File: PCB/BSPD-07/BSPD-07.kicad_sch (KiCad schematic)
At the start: 50 parts, among them IC1 LM393LVQDRQ1, IC2 LM393LVQDRQ1, IC3 LM393LVQDRQ1, IC4 LDO40LPU50RY, IC5 74LVC1G02GW-Q100H, J1 DTM13-12PA, Q1 RSQ025P03HZGTR, Q2 RJU002N06FRAT106, Q3 RJU002N06FRAT106, U2 TLP175A / COMUS AB38-Q

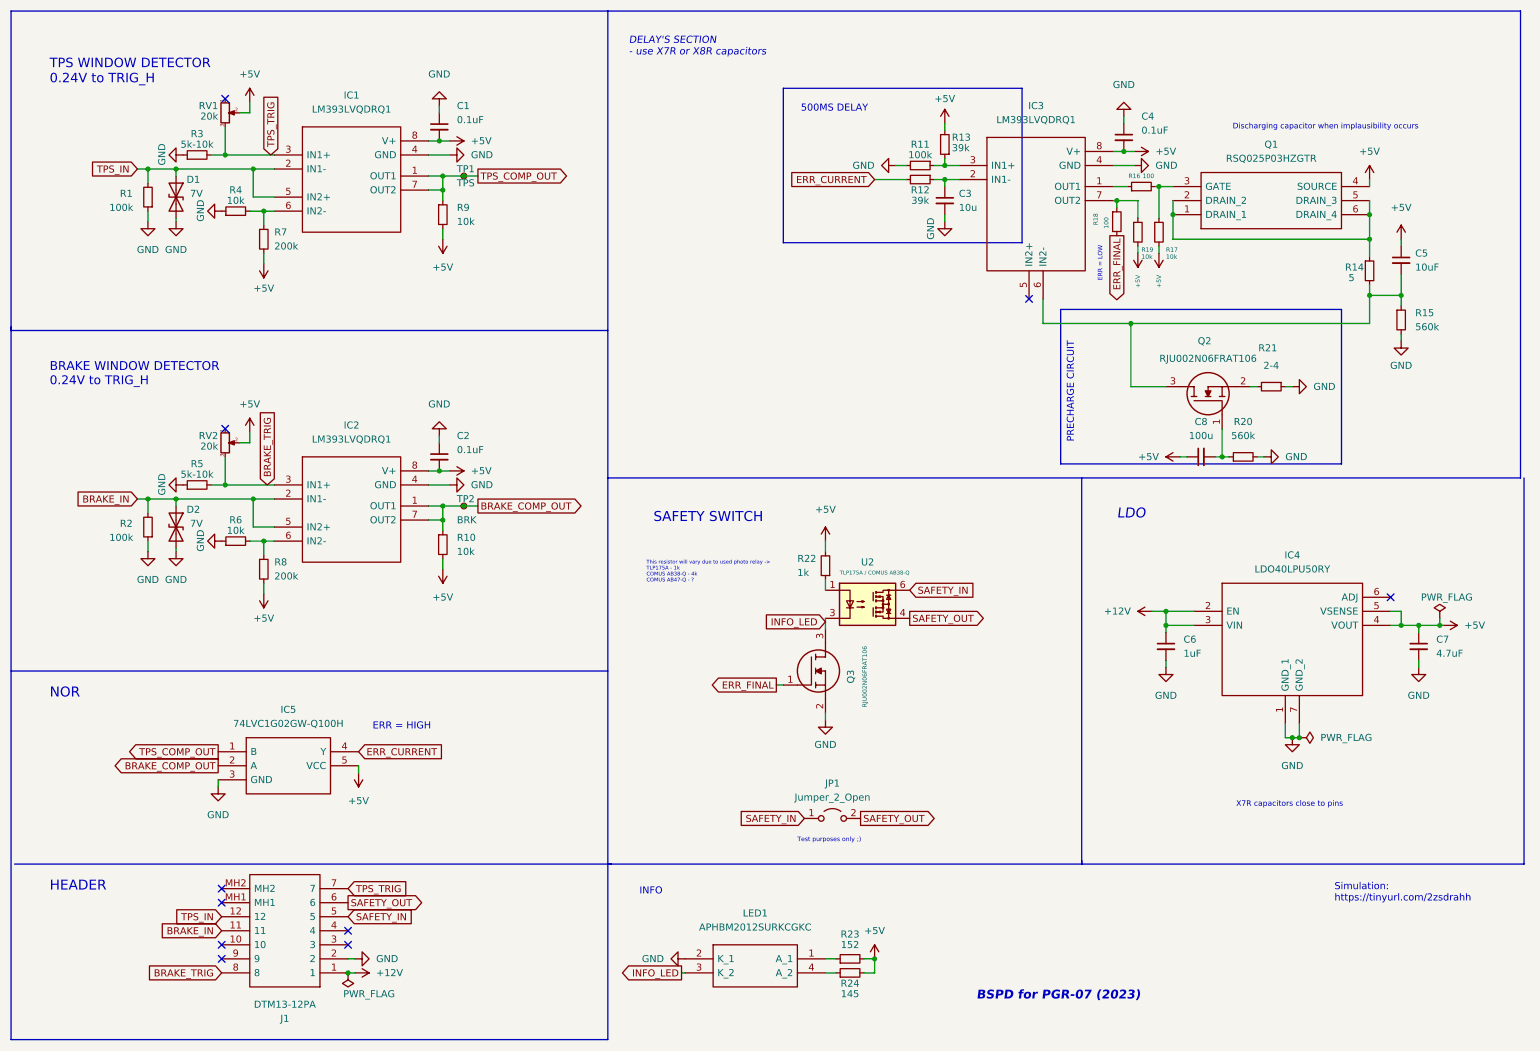
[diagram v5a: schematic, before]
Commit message: Fixed delay resistor reference value
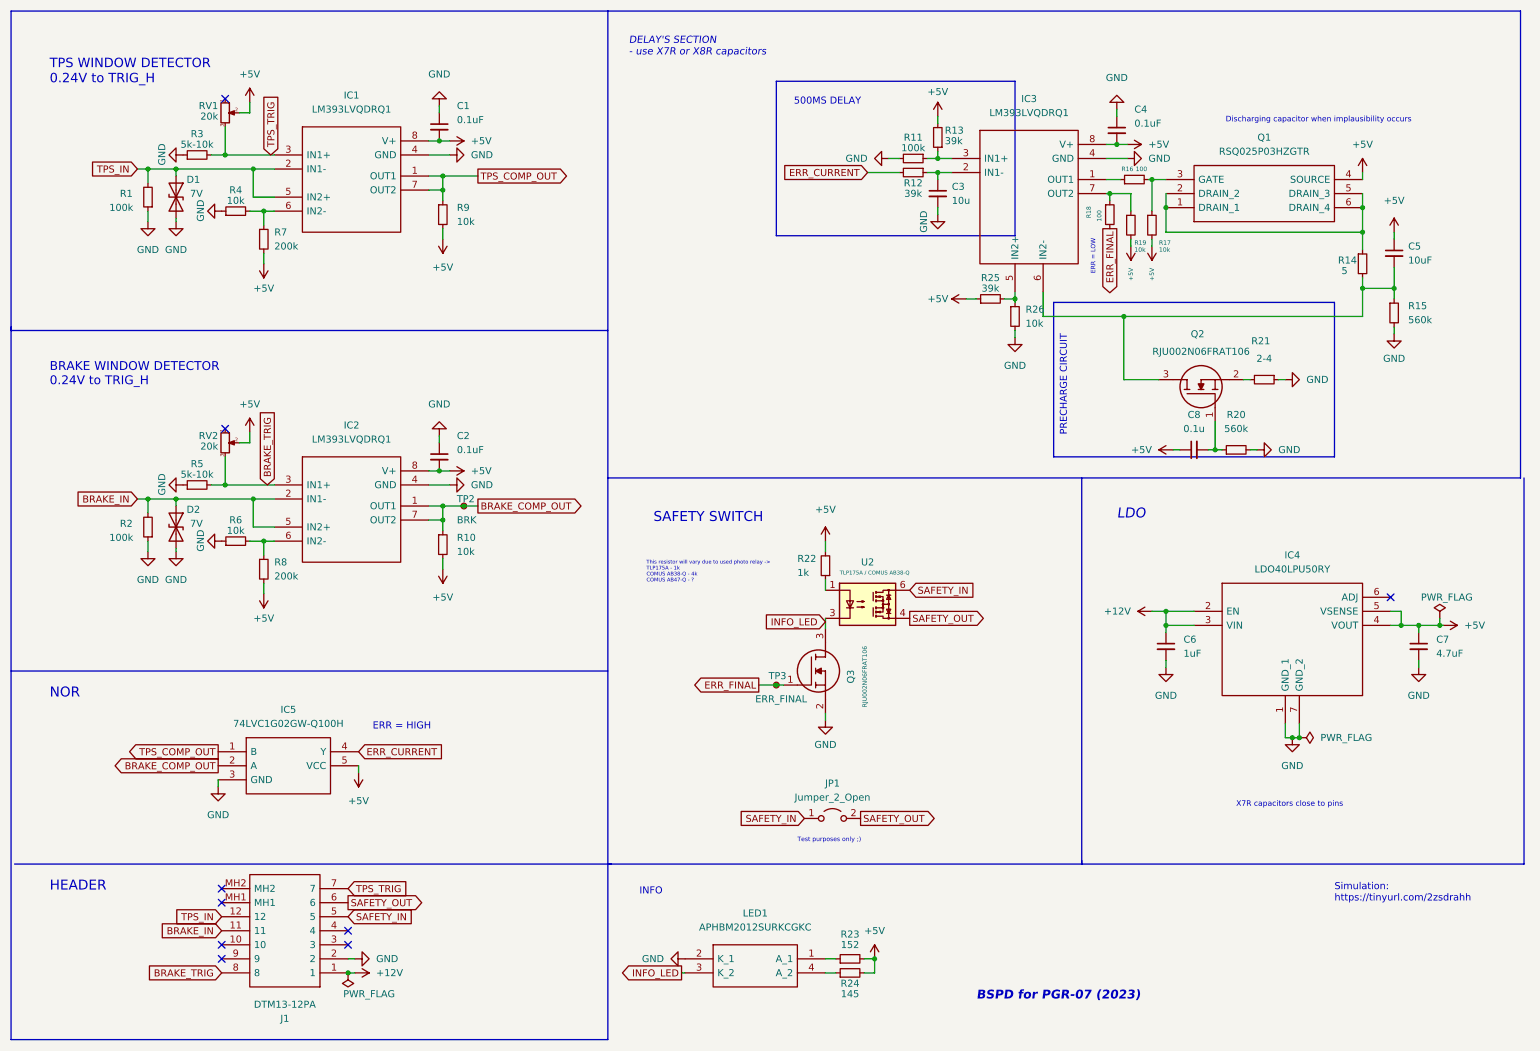
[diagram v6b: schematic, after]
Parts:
- removed TP1: TPS, symbol Connector:TestPoint_Small
- added R25: 39k, Resistor_SMD:R_0402_1005Metric, symbol Device:R_Small
- added R26: 10k, Resistor_SMD:R_0402_1005Metric, symbol Device:R_Small
- added TP3: ERR_FINAL, TestPoint:TestPoint_Pad_D1.0mm, symbol Connector:TestPoint_Small
- C8: value 100u -> 0.1u; footprint (none) -> Capacitor_SMD:C_0402_1005Metric
- LED1: footprint APHBM2012SURKCGKC -> BSPD_07:APHBM2012SURKCGKC
- R16, R17, R18, R19, R20, R21, R22, R23, R24: footprint (none) -> Resistor_SMD:R_0402_1005Metric
- TP2: footprint (none) -> TestPoint:TestPoint_Pad_D1.0mm
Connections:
- net +5V: now also R25.1
- net ERR_FINAL: now also TP3.1
- net GND: now also R26.2
- net at IC3.5 (IN2+): now also R25.2, R26.1
- no-connect marks 10 -> 9
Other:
- moved on the sheet: C3, C4, C5, C8, IC3, Q1, Q2, R11, R12, R13, R14, R15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

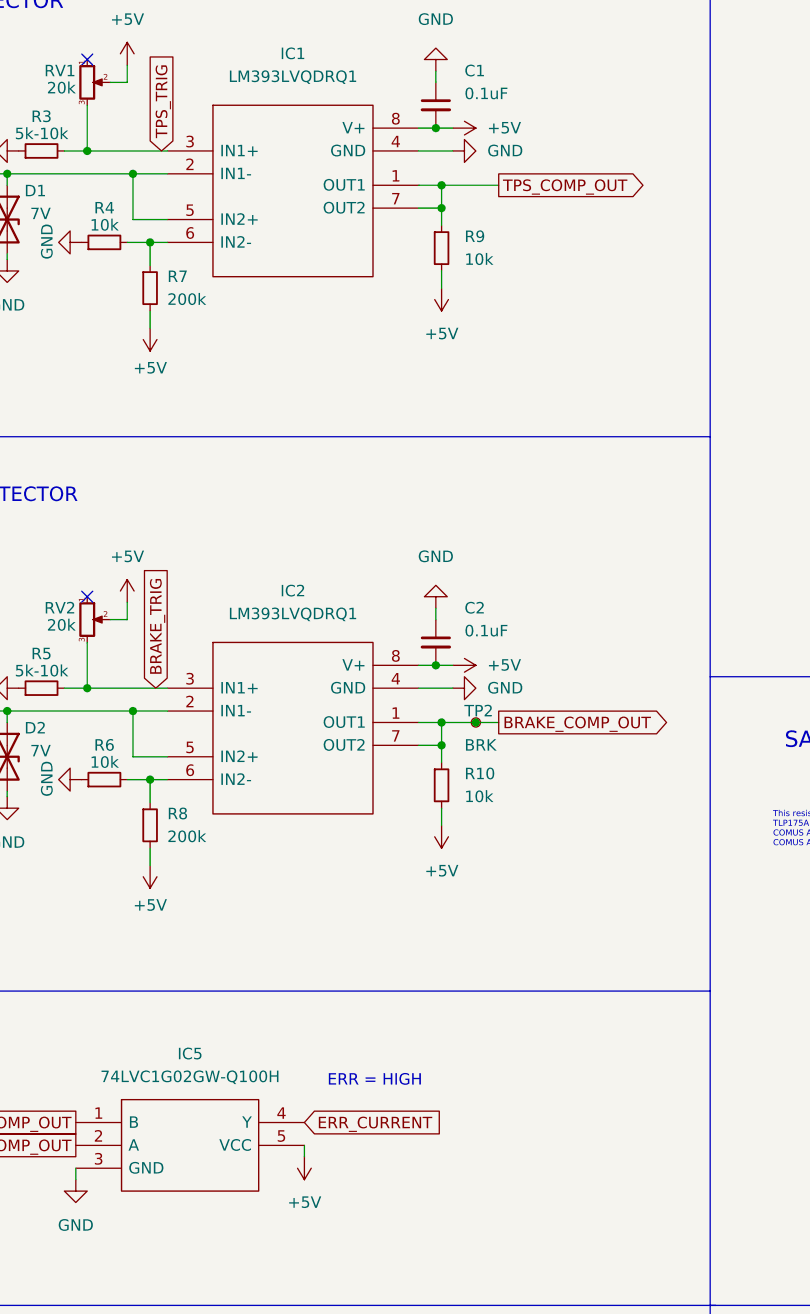
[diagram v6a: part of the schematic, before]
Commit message: Initial board layout with two comparators
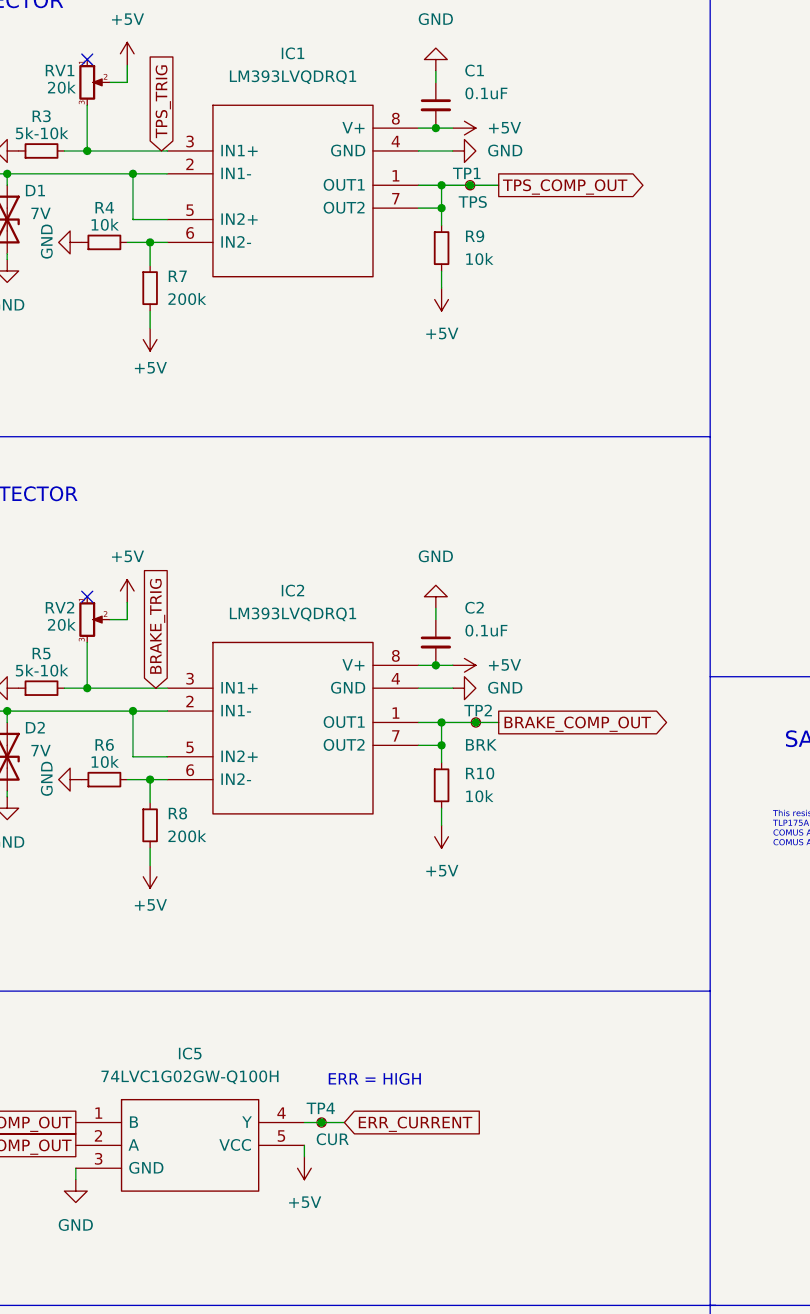
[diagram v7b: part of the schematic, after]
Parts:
- added TP1: TPS, TestPoint:TestPoint_Pad_D1.0mm, symbol Connector:TestPoint_Small
- added TP4: CUR, TestPoint:TestPoint_Pad_D1.0mm, symbol Connector:TestPoint_Small
- D1, D2: footprint (none) -> Diode_SMD:D_0402_1005Metric
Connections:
- net ERR_CURRENT: now also TP4.1
- net TPS_COMP_OUT: now also TP1.1
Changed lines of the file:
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@@
   (junction (at 256.54 62.23) (diameter 0) (color 0 0 0 0)
   )
+  (junction (at 93.345 41.91) (diameter 0) (color 0 0 0 0)
+  )
   (junction (at 168.275 183.515) (diameter 0) (color 0 0 0 0)
   )
@@
   (junction (at 150.495 133.985) (diameter 0) (color 0 0 0 0)
   )
+  (junction (at 76.835 146.05) (diameter 0) (color 0 0 0 0)
+  )
   (junction (at 220.98 47.625) (diameter 0) (color 0 0 0 0)
   )
@@
   (no_connect (at 73.025 180.975))
   (no_connect (at 261.62 118.11))
+  (wire (pts (xy 74.93 146.05) (xy 76.835 146.05))
+    (stroke (width 0) (type default) (color 0 0 0 0))
+  )
   (wire (pts (xy 90.17 41.91) (xy 90.17 44.45))
     (stroke (width 0) (type default) (color 0 0 0 0))
@@
     (stroke (width 0) (type default) (color 0 0 0 0))
   )
+  (wire (pts (xy 93.345 41.91) (xy 96.52 41.91))
+    (stroke (width 0) (type default) (color 0 0 0 0))
+  )
   (wire (pts (xy 256.54 41.275) (xy 256.54 42.545))
     (stroke (width 0) (type default) (color 0 0 0 0))
@@
     (stroke (width 0) (type default) (color 0 0 0 0))
   )
+  (wire (pts (xy 76.835 146.05) (xy 79.375 146.05))
+    (stroke (width 0) (type default) (color 0 0 0 0))
+  )
   (wire (pts (xy 55.88 45.72) (xy 59.69 45.72))
     (stroke (width 0) (type default) (color 0 0 0 0))
@@
     (stroke (width 0) (type default) (color 0 0 0 0))
   )
-  (wire (pts (xy 90.17 41.91) (xy 96.52 41.91))
+  (wire (pts (xy 90.17 41.91) (xy 93.345 41.91))
     (stroke (width 0) (type default) (color 0 0 0 0))
   )
@@
     )
   )
-  (global_label "ERR_CURRENT" (shape input) (at 74.93 146.05 0) (fields_autoplaced)
+  (global_label "ERR_CURRENT" (shape input) (at 79.375 146.05 0) (fields_autoplaced)
     (effects (font (size 1.27 1.27)) (justify left))
-    (property "Intersheet References" "${INTERSHEET_REFS}" (id 0) (at 90.5874 145.9706 0)
+    (property "Intersheet References" "${INTERSHEET_REFS}" (id 0) (at 95.0324 145.9706 0)
       (effects (font (size 1.27 1.27)) (justify left) hide)
     )
@@
     (pin "1")
   )
+  (symbol (lib_id "Connector:TestPoint_Small") (at 76.835 146.05 0) (unit 1)
+    (in_bom yes) (on_board yes)
+    (property "Reference" "TP4" (id 0) (at 75.184 144.526 0)
+      (effects (font (size 1.27 1.27)) (justify left))
+    )
+    (property "Value" "CUR" (id 1) (at 76.2 147.955 0)
+      (effects (font (size 1.27 1.27)) (justify left))
+    )
+    (property "Footprint" "TestPoint:TestPoint_Pad_D1.0mm" (id 2) (at 81.915 146.05 0)
+      (effects (font (size 1.27 1.27)) hide)
+    )
+    (property "Datasheet" "~" (id 3) (at 81.915 146.05 0)
+      (effects (font (size 1.27 1.27)) hide)
+    )
+    (pin "1")
+  )
   (symbol (lib_id "Device:R_Small") (at 215.265 42.545 90) (unit 1)
     (in_bom yes) (on_board yes)
@@
       (effects (font (size 1.27 1.27)) (justify left))
     )
-    (property "Footprint" "" (id 2) (at 41.91 45.72 0)
+    (property "Footprint" "Diode_SMD:D_0402_1005Metric" (id 2) (at 41.91 45.72 0)
       (effects (font (size 1.27 1.27)) hide)
     )
@@
       (effects (font (size 1.27 1.27)) (justify left))
     )
-    (property "Footprint" "" (id 2) (at 41.91 105.41 0)
+    (property "Footprint" "Diode_SMD:D_0402_1005Metric" (id 2) (at 41.91 105.41 0)
       (effects (font (size 1.27 1.27)) hide)
     )
@@
     (pin "1")
   )
+  (symbol (lib_id "Connector:TestPoint_Small") (at 93.345 41.91 0) (unit 1)
+    (in_bom yes) (on_board yes)
+    (property "Reference" "TP1" (id 0) (at 91.44 40.64 0)
+      (effects (font (size 1.27 1.27)) (justify left))
+    )
+    (property "Value" "TPS" (id 1) (at 92.075 43.815 0)
+      (effects (font (size 1.27 1.27)) (justify left))
+    )
+    (property "Footprint" "TestPoint:TestPoint_Pad_D1.0mm" (id 2) (at 98.425 41.91 0)
+      (effects (font (size 1.27 1.27)) hide)
+    )
+    (property "Datasheet" "~" (id 3) (at 98.425 41.91 0)
+      (effects (font (size 1.27 1.27)) hide)
+    )
+    (pin "1")
+  )
   (symbol (lib_id "Connector:TestPoint_Small") (at 150.495 133.985 0) (unit 1)
     (in_bom yes) (on_board yes)
@@
     )
     (path "/d53bf91e-1a8c-4766-8564-0edbccc59e6b"
-      (reference "D1") (unit 1) (value "7V") (footprint "")
+      (reference "D1") (unit 1) (value "7V") (footprint "Diode_SMD:D_0402_1005Metric")
     )
     (path "/ecd71454-9644-4a49-b4a4-82a872eb7f12"
-      (reference "D2") (unit 1) (value "7V") (footprint "")
+      (reference "D2") (unit 1) (value "7V") (footprint "Diode_SMD:D_0402_1005Metric")
     )
     (path "/90a442e5-8955-4be7-a2a2-5ce96ee123ec"
@@
       (reference "RV2") (unit 1) (value "20k") (footprint "BSPD_07:POT-3296X1223LF")
     )
+    (path "/f02257a1-6745-4306-864e-1aad36207a93"
+      (reference "TP1") (unit 1) (value "TPS") (footprint "TestPoint:TestPoint_Pad_D1.0mm")
+    )
     (path "/d2ec44cc-2b00-4640-bd77-87ee1e36d40d"
       (reference "TP2") (unit 1) (value "BRK") (footprint "TestPoint:TestPoint_Pad_D1.0mm")
@@
       (reference "TP3") (unit 1) (value "ERR_FINAL") (footprint "TestPoint:TestPoint_Pad_D1.0mm")
     )
+    (path "/4a20634a-c64f-4da9-b201-d7e7312d786e"
+      (reference "TP4") (unit 1) (value "CUR") (footprint "TestPoint:TestPoint_Pad_D1.0mm")
+    )
     (path "/cbd680d4-2916-4e00-9c09-3a431f6c18e0"
